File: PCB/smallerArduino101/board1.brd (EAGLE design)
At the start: 47.9 x 59.7 mm, 43 parts

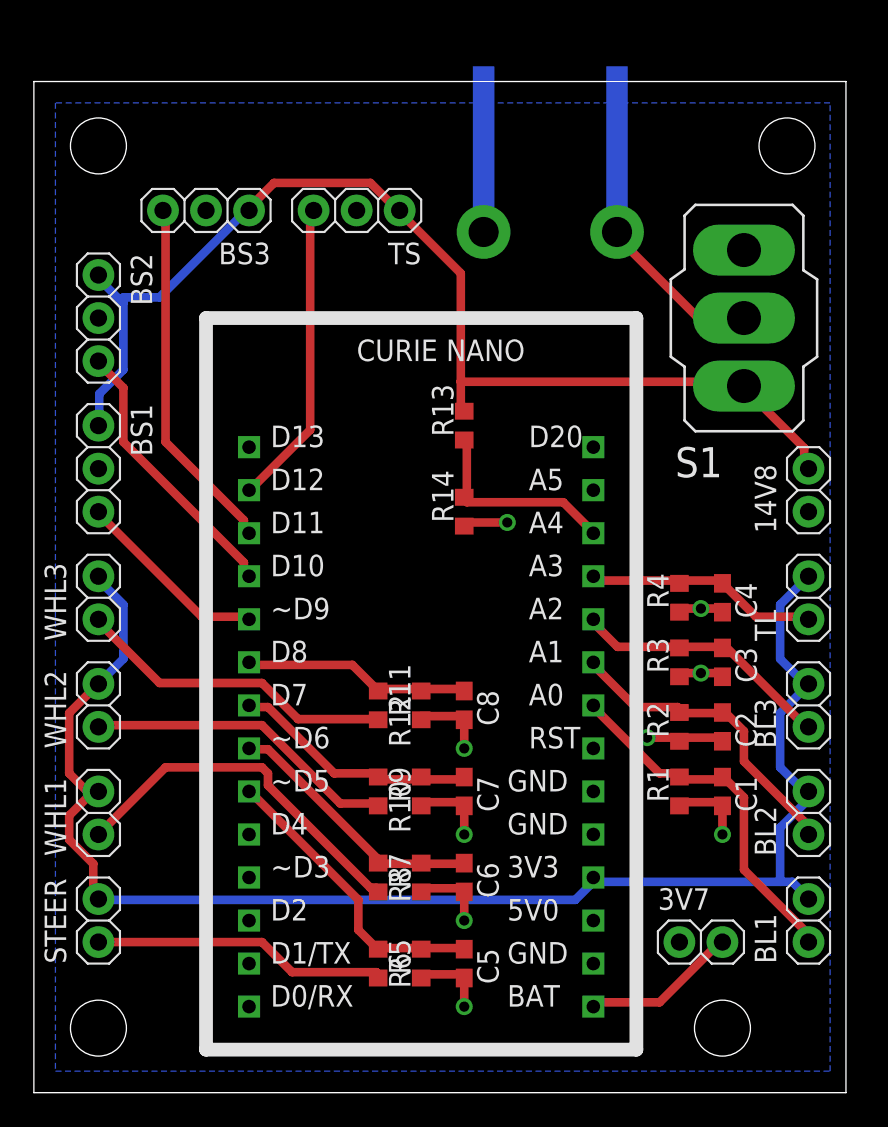
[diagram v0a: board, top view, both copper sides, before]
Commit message: v2 pcb, code for pid, data for pid on bike
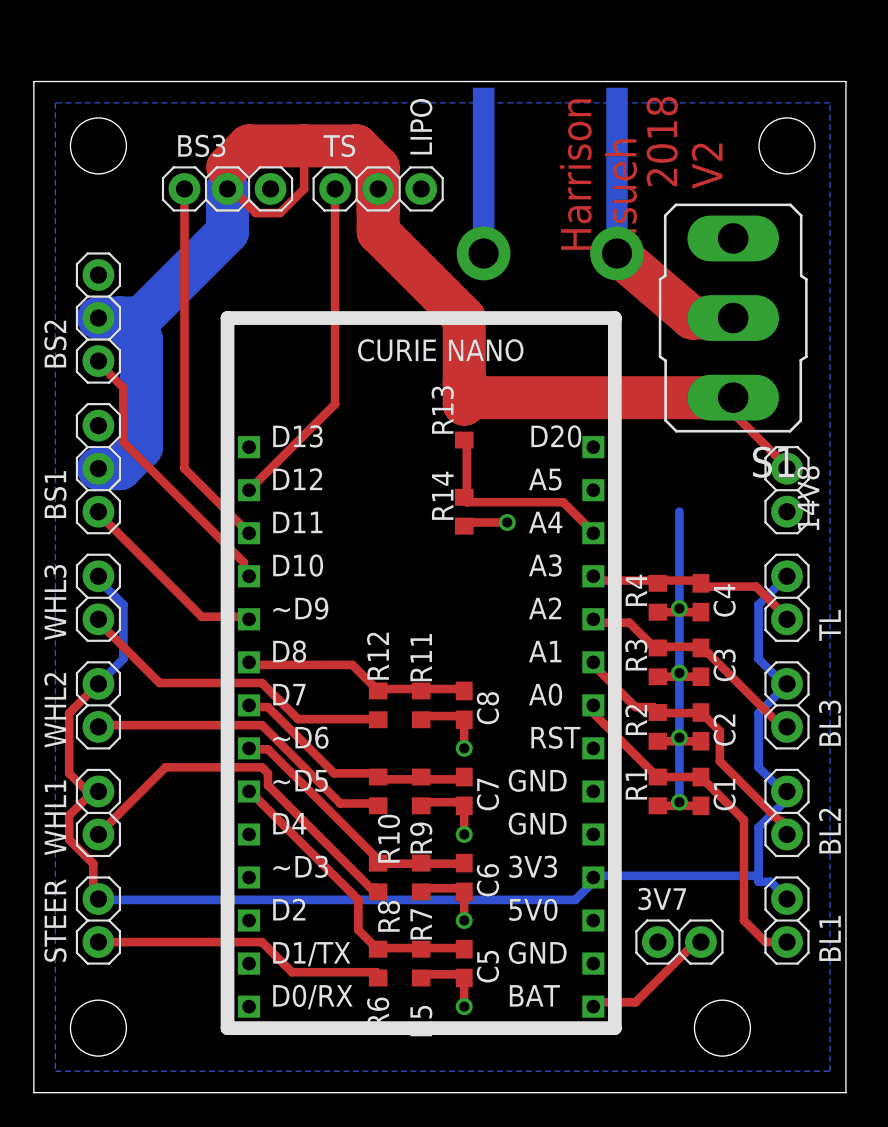
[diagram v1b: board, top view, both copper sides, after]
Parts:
- S1: device switch:320-916 -> switch:M9040P
- moved TS 1.80 mm to (40.6, 53.3)
- moved BS3 1.80 mm to (31.8, 53.3)
- moved 14V8 1.27 mm to (64.8, 35.6)
- moved BL1 1.27 mm to (64.8, 10.2)
- moved BL2 1.27 mm to (64.8, 16.5)
- moved BL3 1.27 mm to (64.8, 22.9)
- moved TL 1.27 mm to (64.8, 29.2)
- moved C1 1.27 mm to (59.7, 17.8)
- moved C2 1.27 mm to (59.7, 21.6)
- moved C3 1.27 mm to (59.7, 25.4)
- moved C4 1.27 mm to (59.7, 29.2)
- moved R1 1.27 mm to (57.1, 17.8)
- moved R2 1.27 mm to (57.1, 21.6)
- moved R3 1.27 mm to (57.1, 25.4)
- moved R4 1.27 mm to (57.1, 29.2)
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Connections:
- net 14V8: now also BS1.2, BS2.2, BS3.2, TS.2; no longer BS1.1, BS2.1, BS3.1, TS.1
- net GND: now also BS1.1, BS2.1, BS3.1, TS.1; no longer BS1.2, BS2.2, BS3.2, TS.2
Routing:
- net 14V8: track 67.0 -> 81.2 mm
- net GND: track 36.9 -> 49.6 mm
- net TILT_PWM: track 18.1 -> 19.9 mm
- net 3V7: track 9.35 -> 8.08 mm
- net 3V3: track 88.4 -> 87.2 mm
- net TILT_P: track 14.0 -> 12.9 mm
- net BRAKE_P3: track 15.5 -> 14.6 mm
- net BRAKE_P1: track 21.6 -> 20.9 mm
- net BRAKE_P2: track 18.5 -> 17.9 mm
- net BRAKE_PWM3: track 21.3 -> 21.9 mm
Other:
- board text added: "2018 V2"
- board text added: "Harrison Hsueh"
